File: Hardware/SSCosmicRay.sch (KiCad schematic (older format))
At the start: 4 parts, among them J2 CONN-9

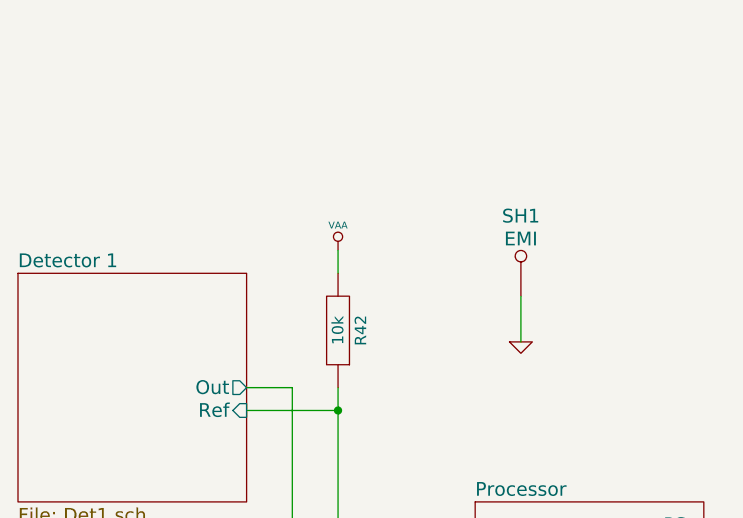
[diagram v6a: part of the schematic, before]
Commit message: Input voltage preregulation to extend input range
Closes #8
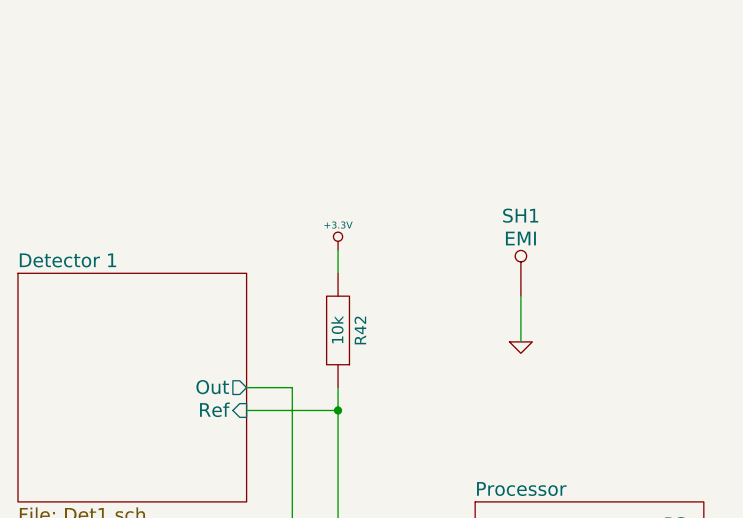
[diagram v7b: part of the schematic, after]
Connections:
- net VAA renamed +3.3V
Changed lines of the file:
@@
 Sheet 1 5
 Title "Solid State Cosmic Ray Detector"
-Date "29 sep 2014"
+Date "29 oct 2014"
 Rev "1"
 Comp "Ethan Harstad"
@@
 	6600 2700 6600 2500
 $Comp
-L VAA #PWR02
-U 1 1 5429C8CD
-P 5800 2300
-F 0 "#PWR02" H 5800 2360 30  0001 C CNN
-F 1 "VAA" H 5800 2410 30  0000 C CNN
-F 2 "" H 5800 2300 60  0000 C CNN
-F 3 "" H 5800 2300 60  0000 C CNN
-	1    5800 2300
-	1    0    0    -1
-$EndComp
-$Comp
-L GND #PWR03
+L GND #PWR02
 U 1 1 5429C942
 P 5800 5500
-F 0 "#PWR03" H 5800 5500 30  0001 C CNN
+F 0 "#PWR02" H 5800 5500 30  0001 C CNN
 F 1 "GND" H 5800 5430 30  0001 C CNN
 F 2 "" H 5800 5500 60  0000 C CNN
@@
 	7400 4300 7900 4300
 $Comp
-L +BATT #PWR04
+L +BATT #PWR03
 U 1 1 5429ECBE
 P 7800 3300
-F 0 "#PWR04" H 7800 3250 20  0001 C CNN
+F 0 "#PWR03" H 7800 3250 20  0001 C CNN
 F 1 "+BATT" H 7800 3400 30  0000 C CNN
 F 2 "" H 7800 3300 60  0000 C CNN
@@
 $EndComp
 $Comp
-L GND #PWR05
+L GND #PWR04
 U 1 1 5429ECCD
 P 7800 4500
-F 0 "#PWR05" H 7800 4500 30  0001 C CNN
+F 0 "#PWR04" H 7800 4500 30  0001 C CNN
 F 1 "GND" H 7800 4430 30  0001 C CNN
 F 2 "" H 7800 4500 60  0000 C CNN
@@
 $EndComp
 $Comp
-L PWR_FLAG #FLG06
+L PWR_FLAG #FLG05
 U 1 1 5429ECDC
 P 8000 3300
-F 0 "#FLG06" H 8000 3395 30  0001 C CNN
+F 0 "#FLG05" H 8000 3395 30  0001 C CNN
 F 1 "PWR_FLAG" H 8000 3480 30  0000 C CNN
 F 2 "" H 8000 3300 60  0000 C CNN
@@
 	8000 3400 7800 3400
 Connection ~ 7800 3400
+$Comp
+L +3.3V #PWR06
+U 1 1 545186E3
+P 5800 2300
+F 0 "#PWR06" H 5800 2260 30  0001 C CNN
+F 1 "+3.3V" H 5800 2410 30  0000 C CNN
+F 2 "" H 5800 2300 60  0000 C CNN
+F 3 "" H 5800 2300 60  0000 C CNN
+	1    5800 2300
+	1    0    0    -1
+$EndComp
 $EndSCHEMATC
